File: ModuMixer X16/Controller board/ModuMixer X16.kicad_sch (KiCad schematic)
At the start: 0 parts

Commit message: idk testing github desktop
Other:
- note added: "TRISOFT H.D/S.D CONFIDENTIAL DO NOT SHARE"
- note removed: "TRISOFT H.D/P.P/S.D CONFIDENTIAL DO NOT SHARE"
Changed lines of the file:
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@@
 		)
 	)
-	(text "TRISOFT H.D/P.P/S.D\n\nCONFIDENTIAL\nDO NOT SHARE"
+	(text "TRISOFT H.D/S.D\n\nCONFIDENTIAL\nDO NOT SHARE"
 		(exclude_from_sim no)
 		(at 11.938 90.678 0)

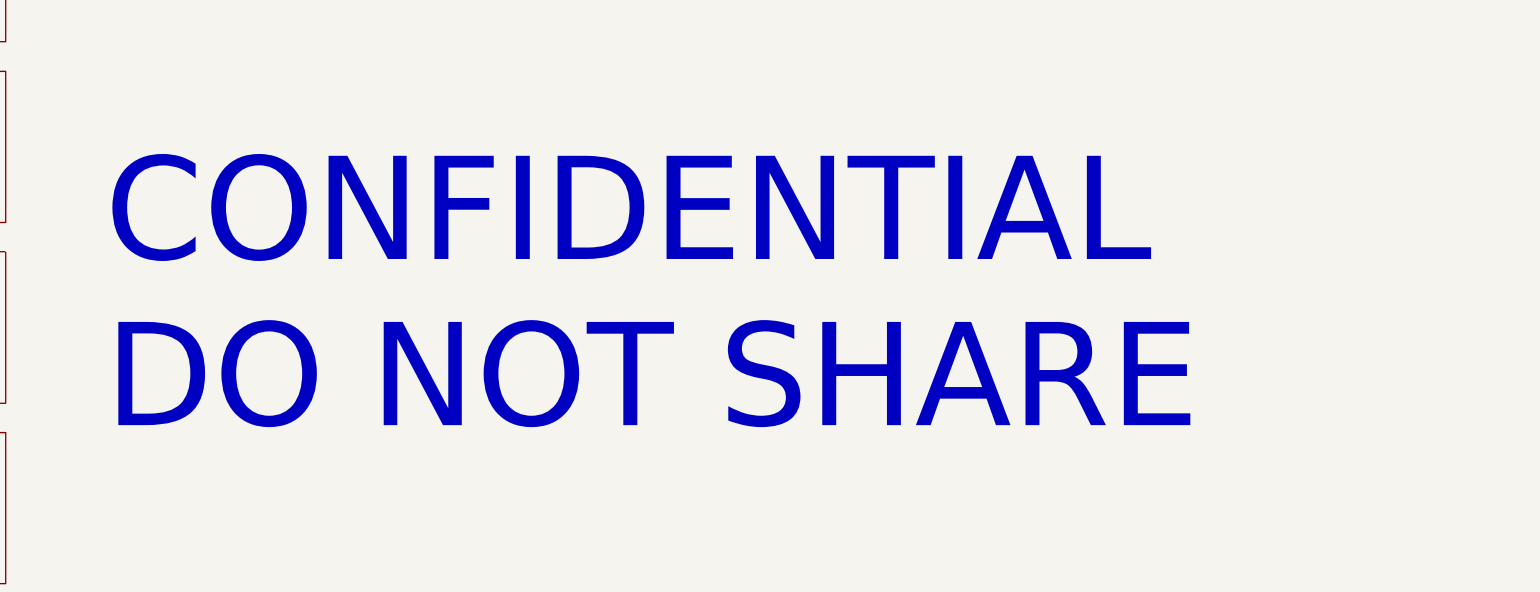
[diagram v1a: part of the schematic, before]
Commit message: Added schematics pdf
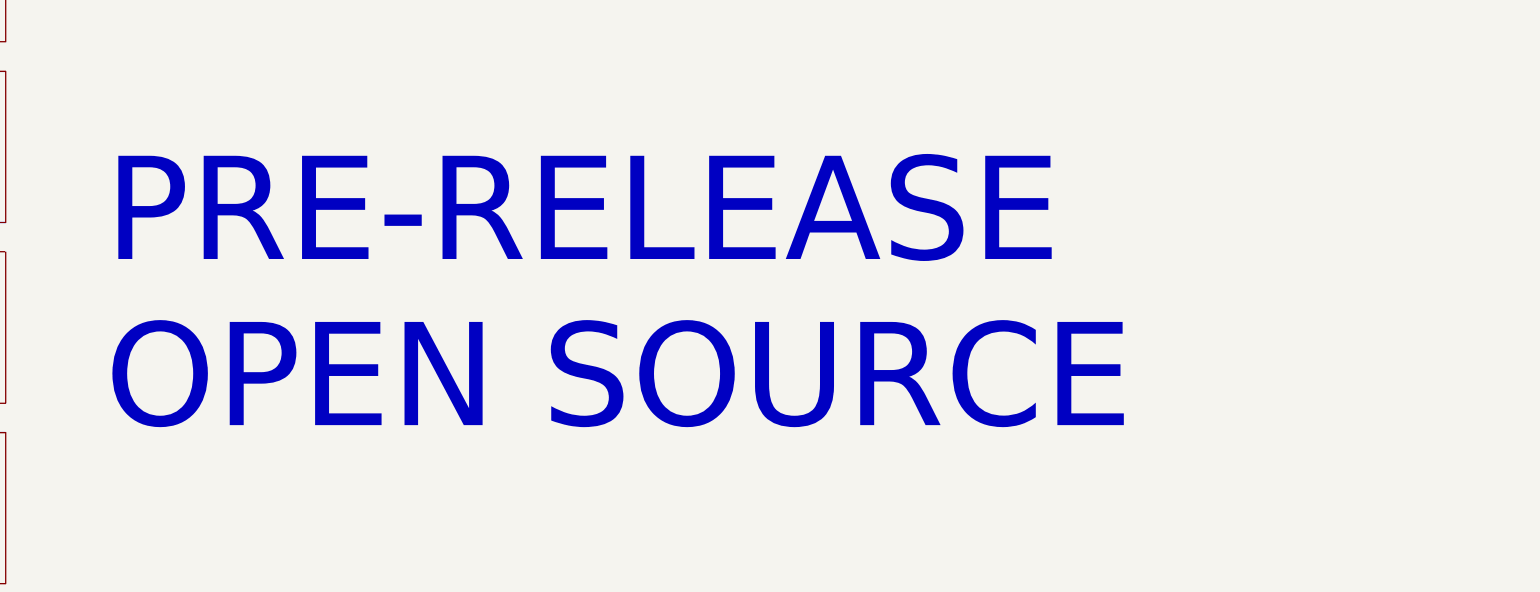
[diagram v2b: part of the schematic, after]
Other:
- note added: "TRISOFT H.D/S.D PRE-RELEASE OPEN SOURCE"
- note removed: "TRISOFT H.D/S.D CONFIDENTIAL DO NOT SHARE"
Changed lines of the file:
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@@
 		)
 	)
-	(text "TRISOFT H.D/S.D\n\nCONFIDENTIAL\nDO NOT SHARE"
+	(text "TRISOFT H.D/S.D\n\nPRE-RELEASE\nOPEN SOURCE"
 		(exclude_from_sim no)
 		(at 11.938 90.678 0)
